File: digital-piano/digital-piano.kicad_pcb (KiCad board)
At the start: 2 copper layers, 116.8 x 71.1 mm, 20 parts, among them J1 Conn_01x22, J10 Conn_01x01, J11 Conn_01x01, J12 Conn_01x01, J13 Conn_01x01, J14 Conn_01x01, J15 Conn_01x01, J16 Conn_01x01, J2 Conn_01x22, J3 Conn_01x01, J4 Conn_01x01, J5 Conn_01x01, J6 Conn_01x01, J7 Conn_01x01, J8 Conn_01x01, J9 Conn_01x01

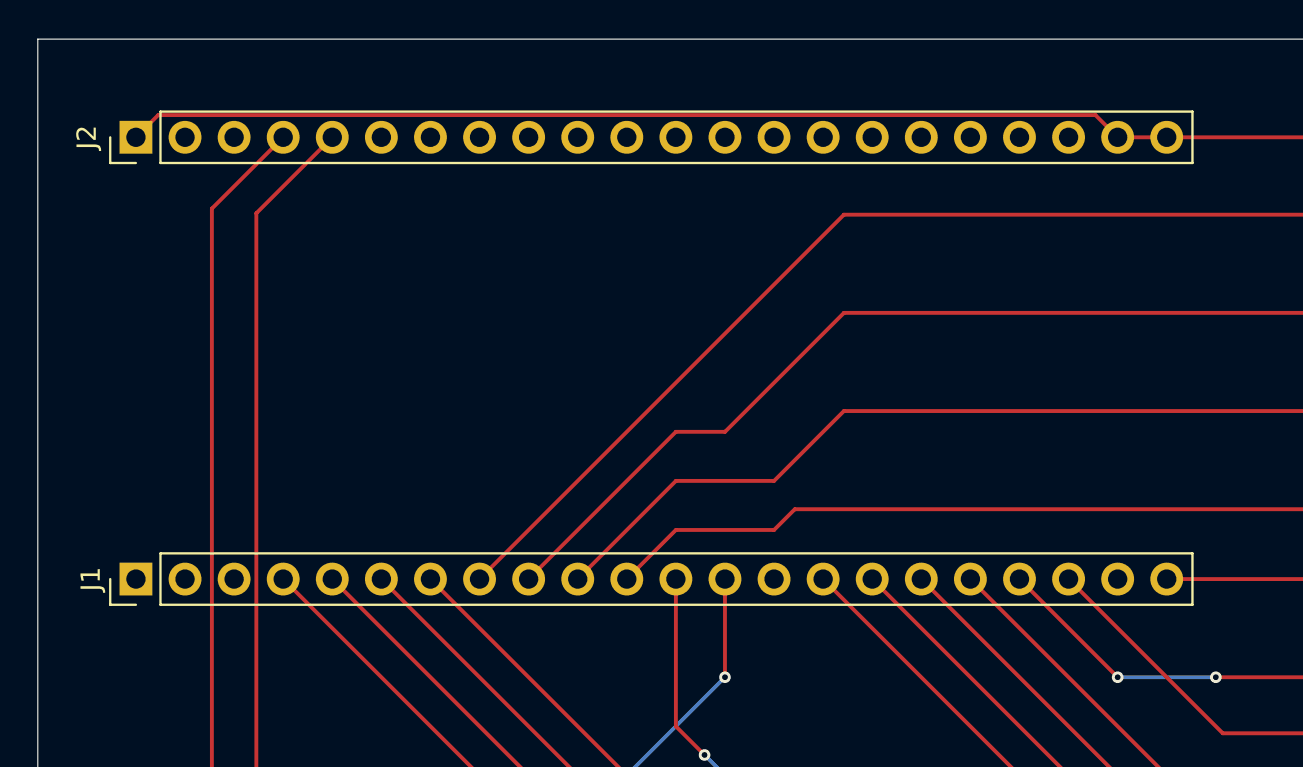
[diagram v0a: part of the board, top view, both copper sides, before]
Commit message: Add Silkscreen to be able to identify board direction
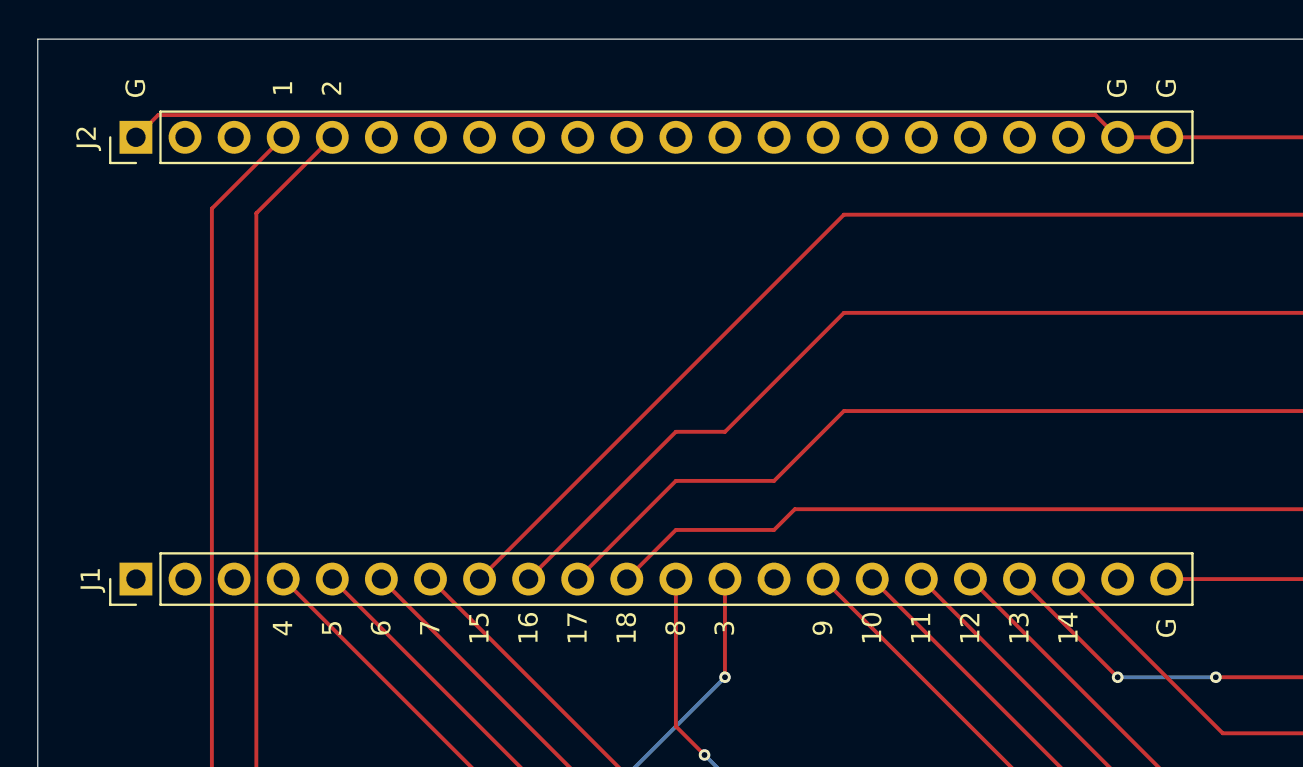
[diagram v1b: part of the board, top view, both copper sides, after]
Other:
- board text added: "1"
- board text added: "10"
- board text added: "11"
- board text added: "12"
- board text added: "13"
- board text added: "14"
- board text added: "15"
- board text added: "16"
- board text added: "17"
- board text added: "18"
- board text added: "2"
- board text added: "3"
- board text added: "4"
- board text added: "5"
- board text added: "6"
- board text added: "7"
- board text added: "8"
- board text added: "9"
- board text added: "G"
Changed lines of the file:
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@@
 		(layer "Edge.Cuts")
+	)
+	(gr_text "16"
+		(at 43.18 60.96 90)
+		(layer "F.SilkS")
+		(effects
+			(font
+				(size 1 1)
+				(thickness 0.1)
+			)
+		)
+	)
+	(gr_text "18"
+		(at 48.26 60.96 90)
+		(layer "F.SilkS")
+		(effects
+			(font
+				(size 1 1)
+				(thickness 0.1)
+			)
+		)
+	)
+	(gr_text "14"
+		(at 71.12 60.96 90)
+		(layer "F.SilkS")
+		(effects
+			(font
+				(size 1 1)
+				(thickness 0.1)
+			)
+		)
+	)
+	(gr_text "G"
+		(at 76.2 33.02 90)
+		(layer "F.SilkS")
+		(effects
+			(font
+				(size 1 1)
+				(thickness 0.1)
+			)
+		)
+	)
+	(gr_text "5"
+		(at 33.02 60.96 90)
+		(layer "F.SilkS")
+		(effects
+			(font
+				(size 1 1)
+				(thickness 0.1)
+			)
+		)
+	)
+	(gr_text "17"
+		(at 45.72 60.96 90)
+		(layer "F.SilkS")
+		(effects
+			(font
+				(size 1 1)
+				(thickness 0.1)
+			)
+		)
+	)
+	(gr_text "6"
+		(at 35.56 60.96 90)
+		(layer "F.SilkS")
+		(effects
+			(font
+				(size 1 1)
+				(thickness 0.1)
+			)
+		)
+	)
+	(gr_text "13"
+		(at 68.58 60.96 90)
+		(layer "F.SilkS")
+		(effects
+			(font
+				(size 1 1)
+				(thickness 0.1)
+			)
+		)
+	)
+	(gr_text "2"
+		(at 33.02 33.02 90)
+		(layer "F.SilkS")
+		(effects
+			(font
+				(size 1 1)
+				(thickness 0.1)
+			)
+		)
+	)
+	(gr_text "1"
+		(at 30.48 33.02 90)
+		(layer "F.SilkS")
+		(effects
+			(font
+				(size 1 1)
+				(thickness 0.1)
+			)
+		)
+	)
+	(gr_text "G"
+		(at 73.66 33.02 90)
+		(layer "F.SilkS")
+		(effects
+			(font
+				(size 1 1)
+				(thickness 0.1)
+			)
+		)
+	)
+	(gr_text "7"
+		(at 38.1 60.96 90)
+		(layer "F.SilkS")
+		(effects
+			(font
+				(size 1 1)
+				(thickness 0.1)
+			)
+		)
+	)
+	(gr_text "10"
+		(at 60.96 60.96 90)
+		(layer "F.SilkS")
+		(effects
+			(font
+				(size 1 1)
+				(thickness 0.1)
+			)
+		)
+	)
+	(gr_text "3"
+		(at 53.34 60.96 90)
+		(layer "F.SilkS")
+		(effects
+			(font
+				(size 1 1)
+				(thickness 0.1)
+			)
+		)
+	)
+	(gr_text "4"
+		(at 30.48 60.96 90)
+		(layer "F.SilkS")
+		(effects
+			(font
+				(size 1 1)
+				(thickness 0.1)
+			)
+		)
+	)
+	(gr_text "G"
+		(at 76.2 60.96 90)
+		(layer "F.SilkS")
+		(effects
+			(font
+				(size 1 1)
+				(thickness 0.1)
+			)
+		)
+	)
+	(gr_text "G"
+		(at 22.86 33.02 90)
+		(layer "F.SilkS")
+		(effects
+			(font
+				(size 1 1)
+				(thickness 0.1)
+			)
+		)
+	)
+	(gr_text "9"
+		(at 58.42 60.96 90)
+		(layer "F.SilkS")
+		(effects
+			(font
+				(size 1 1)
+				(thickness 0.1)
+			)
+		)
+	)
+	(gr_text "8"
+		(at 50.8 60.96 90)
+		(layer "F.SilkS")
+		(effects
+			(font
+				(size 1 1)
+				(thickness 0.1)
+			)
+		)
+	)
+	(gr_text "11"
+		(at 63.5 60.96 90)
+		(layer "F.SilkS")
+		(effects
+			(font
+				(size 1 1)
+				(thickness 0.1)
+			)
+		)
+	)
+	(gr_text "15"
+		(at 40.64 60.96 90)
+		(layer "F.SilkS")
+		(effects
+			(font
+				(size 1 1)
+				(thickness 0.1)
+			)
+		)
+	)
+	(gr_text "12"
+		(at 66.04 60.96 90)
+		(layer "F.SilkS")
+		(effects
+			(font
+				(size 1 1)
+				(thickness 0.1)
+			)
+		)
 	)
 	(segment
